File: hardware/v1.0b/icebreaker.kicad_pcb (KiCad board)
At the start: 4 copper layers, 73 x 37 mm, 128 parts, among them J1 Jumper, J10 Jumper, J11 Jumper, J12 Jumper, J13 Jumper, J14 Jumper, J15 Jumper, J16 Jumper, J17 Jumper, J18 Jumper, J19 Jumper, J2 Jumper, J20 Flash, J21 PMOD, J22 PMOD, J23 PMOD, J24 PMOD, J25 RGB Led, J26 5V AUX, J27 5V AUX, J28 CRESET, J3 Jumper, J4 Jumper, J5 Jumper, J6 Jumper, J7 Jumper, J8 Jumper, J9 Jumper, P1 pkl_USB_OTG, P2 UP, P3 UP, P4 UP, P5 UP, SW1 TACT, SW2 TACT, SW3 TACT, SW4 TACT, U1 93C46B-SOT-23-6, U2 3.3V, U3 1V2, U4 FT2232H, U5 W25Q, U6 ICE5LP4K-SG48, U7 12MHz

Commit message: Fixed pin header 3d models.
We had some of the models doubled up or not fully disabled. Now the TH
pin headers are all using KiCad V5 3d model locations and are all
disabled.

This fixes #23
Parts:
- removed the REF** at (42.2, 47.2)
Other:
- board text removed: "1Bitsquared"
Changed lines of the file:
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@@
-(kicad_pcb (version 20171130) (host pcbnew 5.0.0-fee4fd1~66~ubuntu18.04.1)
+(kicad_pcb (version 20171130) (host pcbnew 5.1.2-f72e74a~84~ubuntu18.04.1)
   (general
     (thickness 1.6)
-    (drawings 337)
+    (drawings 336)
     (tracks 1478)
     (zones 0)
-    (modules 128)
+    (modules 127)
     (nets 134)
   )
@@
     (zone_45_only yes)
     (trace_min 0.149)
-    (segment_width 0.2)
-    (edge_width 0.15)
     (via_size 0.5)
     (via_drill 0.3)
@@
     (uvia_min_size 0.2)
     (uvia_min_drill 0.1)
+    (edge_width 0.15)
+    (segment_width 0.2)
     (pcb_text_width 0.3)
     (pcb_text_size 1.5 1.5)
@@
     (pad_drill 0)
     (pad_to_mask_clearance 0.05)
+    (solder_mask_min_width 0.25)
     (aux_axis_origin 0 0)
     (grid_origin 55.1 47.5)
-    (visible_elements FFFFFF1F)
+    (visible_elements FFFFEF1F)
     (pcbplotparams
       (layerselection 0x010fc_ffffffff)
@@
       (rotate (xyz 0 0 0))
     )
+    (model ${KIPRJMOD}/../../lib/pkl/packages3d/pkl_buttons_switches.3dshapes/PTS810SJG250SMTRLFS.stp
+      (offset (xyz 0 0 1.5))
+      (scale (xyz 1 1 1))
+      (rotate (xyz -90 0 0))
+    )
   )
   (module pkl_buttons_switches:SW_SPST_3x4x2.5 (layer F.Cu)
@@
       (rotate (xyz 0 0 0))
     )
+    (model ${KIPRJMOD}/../../lib/pkl/packages3d/pkl_buttons_switches.3dshapes/PTS810SJG250SMTRLFS.stp
+      (offset (xyz 0 0 1.5))
+      (scale (xyz 1 1 1))
+      (rotate (xyz -90 0 0))
+    )
   )
   (module pkl_buttons_switches:SW_SPST_3x4x2.5 (layer F.Cu)
@@
       (rotate (xyz 0 0 0))
     )
+    (model ${KIPRJMOD}/../../lib/pkl/packages3d/pkl_buttons_switches.3dshapes/PTS810SJG250SMTRLFS.stp
+      (offset (xyz 0 0 1.5))
+      (scale (xyz 1 1 1))
+      (rotate (xyz -90 0 0))
+    )
   )
   (module pkl_buttons_switches:SW_SPST_3x4x2.5 (layer F.Cu)
@@
       (rotate (xyz 0 0 0))
     )
+    (model ${KIPRJMOD}/../../lib/pkl/packages3d/pkl_buttons_switches.3dshapes/PTS810SJG250SMTRLFS.stp
+      (offset (xyz 0 0 1.5))
+      (scale (xyz 1 1 1))
+      (rotate (xyz -90 0 0))
+    )
   )
   (module pkl_jumpers:J_NCNO_0903_30 (layer B.Cu)
@@
     (pad 7 thru_hole oval (at 0 15.24 90) (size 2.032 1.7272) (drill 1.016) (layers *.Cu *.Mask)
       (net 26 GND))
-    (model Pin_Headers.3dshapes/Pin_Header_Straight_1x07.wrl
-      (offset (xyz 0 -7.619999885559082 0))
+    (model ${KISYS3DMOD}/Connector_PinHeader_2.54mm.3dshapes/PinHeader_1x07_P2.54mm_Vertical.stepX
+      (at (xyz 0 0 0))
       (scale (xyz 1 1 1))
-      (rotate (xyz 0 0 90))
+      (rotate (xyz 0 0 0))
     )
   )
@@
     (pad 8 thru_hole oval (at 2.54 7.62 90) (size 1.7272 1.7272) (drill 1.016) (layers *.Cu *.Mask)
       (net 3 +3V3))
-    (model Pin_Headers.3dshapes/Pin_Header_Straight_2x04.wrl
-      (offset (xyz 1.269999980926514 -3.809999942779541 0))
+    (model ${KISYS3DMOD}/Connector_PinHeader_2.54mm.3dshapes/PinHeader_2x04_P2.54mm_Vertical.stepX
+      (at (xyz 0 0 0))
       (scale (xyz 1 1 1))
-      (rotate (xyz 0 0 90))
+      (rotate (xyz 0 0 0))
     )
   )
@@
     (pad 1 thru_hole rect (at 0 0 270) (size 1.7 1.7) (drill 1) (layers *.Cu *.Mask)
       (net 44 /iCE_CRESET))
-    (model ${KISYS3DMOD}/Connector_PinHeader_2.54mm.3dshapes/PinHeader_2x01_P2.54mm_VerticalX.wrl
+    (model ${KISYS3DMOD}/Connector_PinHeader_2.54mm.3dshapes/PinHeader_2x01_P2.54mm_Vertical.stepX
       (at (xyz 0 0 0))
       (scale (xyz 1 1 1))
@@
     (pad 2 thru_hole oval (at 2.54 0) (size 1.7272 1.7272) (drill 1.016) (layers *.Cu *.Mask)
       (net 26 GND))
-    (model Pin_Headers.3dshapes/Pin_Header_Straight_2x01.wrl
-      (offset (xyz 1.269999980926514 0 0))
+    (model ${KISYS3DMOD}/Connector_PinSocket_2.54mm.3dshapes/PinSocket_1x02_P2.54mm_Vertical.stepX
+      (at (xyz 0 0 0))
       (scale (xyz 1 1 1))
-      (rotate (xyz 0 0 90))
+      (rotate (xyz 0 0 -90))
     )
   )
@@
     (pad 2 thru_hole oval (at 2.54 0 90) (size 1.7272 1.7272) (drill 1.016) (layers *.Cu *.Mask)
       (net 26 GND))
-    (model Pin_Headers.3dshapes/Pin_Header_Straight_2x01.wrl
-      (offset (xyz 1.269999980926514 0 0))
+    (model ${KISYS3DMOD}/Connector_PinSocket_2.54mm.3dshapes/PinSocket_1x02_P2.54mm_Vertical.stepX
+      (at (xyz 0 0 0))
       (scale (xyz 1 1 1))
-      (rotate (xyz 0 0 90))
+      (rotate (xyz 0 0 -90))
     )
   )
@@
     (pad 7 thru_hole oval (at 2.54 12.7 180) (size 1.7272 1.7272) (drill 1.016) (layers *.Cu *.Mask)
       (net 107 /P2_7x))
-    (model Pin_Headers.3dshapes/Pin_Header_Straight_2x06.wrl
-      (offset (xyz 1.269999980926514 -6.349999904632568 0))
+    (model ${KISYS3DMOD}/Connector_PinHeader_2.54mm.3dshapes/PinHeader_2x06_P2.54mm_Horizontal.stepX
+      (at (xyz 0 0 0))
       (scale (xyz 1 1 1))
-      (rotate (xyz 0 0 90))
+      (rotate (xyz 0 0 0))
     )
   )
@@
     (pad 7 thru_hole oval (at 12.7 2.54 90) (size 1.7272 1.7272) (drill 1.016) (layers *.Cu *.Mask)
       (net 107 /P2_7x))
-    (model Socket_Strips.3dshapes/Socket_Strip_Straight_2x06.wrl
-      (offset (xyz 6.349999904632568 -1.269999980926514 0))
+    (model ${KISYS3DMOD}/Connector_PinSocket_2.54mm.3dshapes/PinSocket_2x06_P2.54mm_Horizontal.stepX
+      (at (xyz 0 0 0))
       (scale (xyz 1 1 1))
-      (rotate (xyz 0 0 180))
+      (rotate (xyz 0 0 -90))
     )
   )
@@
     (pad 6 thru_hole circle (at 0 0 180) (size 1.7272 1.7272) (drill 1.016) (layers *.Cu *.Mask)
       (net 3 +3V3))
-    (model dis${KISYS3DMOD}/Connector_PinSocket_2.54mm.3dshapes/PinSocket_2x06_P2.54mm_Horizontal.step
+    (model ${KISYS3DMOD}/Connector_PinSocket_2.54mm.3dshapes/PinSocket_2x06_P2.54mm_Horizontal.stepX
       (at (xyz 0 0 0))
       (scale (xyz 1 1 1))
@@
     (pad 7 thru_hole oval (at 12.7 2.54 180) (size 1.7272 1.7272) (drill 1.016) (layers *.Cu *.Mask)
       (net 93 /P1A7x))
-    (model dis${KISYS3DMOD}/Connector_PinSocket_2.54mm.3dshapes/PinSocket_2x06_P2.54mm_Horizontal.step
-      (offset (xyz 6.35 -1.27 0))
+    (model ${KISYS3DMOD}/Connector_PinSocket_2.54mm.3dshapes/PinSocket_2x06_P2.54mm_Horizontal.stepX
+      (at (xyz 0 0 0))
       (scale (xyz 1 1 1))
       (rotate (xyz 0 0 -90))
@@
       (net 6 /xFIFO_WKUP))
   )
-  (module pkl_logos:1b2_Logo_SilkS_5mm locked (layer B.Cu)
-    (at 42.2 47.2 180)
-    (fp_text reference REF** (at 0 -4 180) (layer B.Fab) hide
-      (effects (font (size 1 1) (thickness 0.15)) (justify mirror))
-    )
-    (fp_text value 1b2_Logo_SilkS_5mm (at 0 4 180) (layer B.Fab) hide
-      (effects (font (size 1 1) (thickness 0.15)) (justify mirror))
-    )
-    (fp_line (start -0.5 0.5) (end -0.5 2.5) (layer B.SilkS) (width 0.2))
-    (fp_line (start -0.5 2.5) (end -2.5 2.5) (layer B.SilkS) (width 0.2))
-    (fp_line (start -2.5 2.5) (end -2.5 0.5) (layer B.SilkS) (width 0.2))
-    (fp_line (start -2.5 0.5) (end -0.5 0.5) (layer B.SilkS) (width 0.2))
-    (fp_line (start -0.5 2.5) (end 0 2) (layer B.SilkS) (width 0.2))
-    (fp_line (start 0 2) (end 0 0) (layer B.SilkS) (width 0.2))
-    (fp_line (start 0 0) (end -0.5 0.5) (layer B.SilkS) (width 0.2))
-    (fp_line (start -2.5 0.5) (end -2 0) (layer B.SilkS) (width 0.2))
-    (fp_line (start -2 0) (end 0 0) (layer B.SilkS) (width 0.2))
-    (fp_line (start 2 2) (end 0.5 2) (layer B.SilkS) (width 0.2))
-    (fp_line (start 0.5 2) (end 0.5 -0.5) (layer B.SilkS) (width 0.2))
-    (fp_line (start 0.5 -0.5) (end -2 -0.5) (layer B.SilkS) (width 0.2))
-    (fp_line (start -2 -0.5) (end -2 -2) (layer B.SilkS) (width 0.2))
-    (fp_line (start -2 -2) (end 2 -2) (layer B.SilkS) (width 0.2))
-    (fp_line (start 2 -2) (end 2 2) (layer B.SilkS) (width 0.2))
-    (fp_line (start 2 2) (end 2.5 1.5) (layer B.SilkS) (width 0.2))
-    (fp_line (start 2.5 1.5) (end 2.5 -2.5) (layer B.SilkS) (width 0.2))
-    (fp_line (start 2.5 -2.5) (end 2 -2) (layer B.SilkS) (width 0.2))
-    (fp_line (start -2 -2) (end -1.5 -2.5) (layer B.SilkS) (width 0.2))
-    (fp_line (start -1.5 -2.5) (end 2.5 -2.5) (layer B.SilkS) (width 0.2))
-  )
   (module pkl_dipol:R_Array_Convex_4x0402 (layer F.Cu)
     (at 57.105546 43.866206 135)
@@
   (module pkl_connectors:Connector_USB_Micro_B_SMD locked (layer F.Cu)
     (at 31.5 47.5 180)
+    (attr smd)
     (fp_text reference P1 (at 4 0 270) (layer F.Fab)
       (effects (font (size 1 1) (thickness 0.15)))
@@
     (effects (font (size 0.75 0.75) (thickness 0.1875)))
   )
-  (gr_text 1Bitsquared (at 42.1 51) (layer B.SilkS)
-    (effects (font (size 1 1) (thickness 0.25)) (justify mirror))
-  )
   (gr_text CDONE (at 56.7 56.7) (layer F.SilkS)

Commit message: Added more legend silkscreen to ears.
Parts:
- added REF**: 1b2_Logo_SilkS_5mm, pkl_logos:1b2_Logo_SilkS_5mm, B.Cu at (42.2, 47.2)
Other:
- board text added: "1Bitsquared"
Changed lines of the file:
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@@
   (general
     (thickness 1.6)
-    (drawings 336)
+    (drawings 337)
     (tracks 1478)
     (zones 0)
-    (modules 127)
+    (modules 128)
     (nets 134)
   )
@@
     (add_net "Net-(U7-Pad2)")
   )
+  (module pkl_logos:1b2_Logo_SilkS_5mm locked (layer B.Cu)
+    (at 42.2 47.2 180)
+    (fp_text reference REF** (at 0 -4 180) (layer B.Fab) hide
+      (effects (font (size 1 1) (thickness 0.15)) (justify mirror))
+    )
+    (fp_text value 1b2_Logo_SilkS_5mm (at 0 4 180) (layer B.Fab) hide
+      (effects (font (size 1 1) (thickness 0.15)) (justify mirror))
+    )
+    (fp_line (start -0.5 0.5) (end -0.5 2.5) (layer B.SilkS) (width 0.2))
+    (fp_line (start -0.5 2.5) (end -2.5 2.5) (layer B.SilkS) (width 0.2))
+    (fp_line (start -2.5 2.5) (end -2.5 0.5) (layer B.SilkS) (width 0.2))
+    (fp_line (start -2.5 0.5) (end -0.5 0.5) (layer B.SilkS) (width 0.2))
+    (fp_line (start -0.5 2.5) (end 0 2) (layer B.SilkS) (width 0.2))
+    (fp_line (start 0 2) (end 0 0) (layer B.SilkS) (width 0.2))
+    (fp_line (start 0 0) (end -0.5 0.5) (layer B.SilkS) (width 0.2))
+    (fp_line (start -2.5 0.5) (end -2 0) (layer B.SilkS) (width 0.2))
+    (fp_line (start -2 0) (end 0 0) (layer B.SilkS) (width 0.2))
+    (fp_line (start 2 2) (end 0.5 2) (layer B.SilkS) (width 0.2))
+    (fp_line (start 0.5 2) (end 0.5 -0.5) (layer B.SilkS) (width 0.2))
+    (fp_line (start 0.5 -0.5) (end -2 -0.5) (layer B.SilkS) (width 0.2))
+    (fp_line (start -2 -0.5) (end -2 -2) (layer B.SilkS) (width 0.2))
+    (fp_line (start -2 -2) (end 2 -2) (layer B.SilkS) (width 0.2))
+    (fp_line (start 2 -2) (end 2 2) (layer B.SilkS) (width 0.2))
+    (fp_line (start 2 2) (end 2.5 1.5) (layer B.SilkS) (width 0.2))
+    (fp_line (start 2.5 1.5) (end 2.5 -2.5) (layer B.SilkS) (width 0.2))
+    (fp_line (start 2.5 -2.5) (end 2 -2) (layer B.SilkS) (width 0.2))
+    (fp_line (start -2 -2) (end -1.5 -2.5) (layer B.SilkS) (width 0.2))
+    (fp_line (start -1.5 -2.5) (end 2.5 -2.5) (layer B.SilkS) (width 0.2))
+  )
   (module pkl_buttons_switches:SW_SPST_3x4x2.5 (layer F.Cu)
     (at 99.4 40.7)
@@
     )
   )
+  (gr_text 1Bitsquared (at 42.1 51) (layer B.SilkS)
+    (effects (font (size 1 1) (thickness 0.25)) (justify mirror))
+  )
   (gr_text 1V8 (at 55.5 47 315) (layer B.SilkS)

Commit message: Replaced/added the null logo to the boards.
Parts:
- REF**: value 1b2_Logo_SilkS_5mm -> null_Logo_SilkS_5mm; footprint pkl_logos:1b2_Logo_SilkS_5mm -> pkl_logos:null_Logo_SilkS_5mm
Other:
- board text added: "NULL"
- board text removed: "1Bitsquared"
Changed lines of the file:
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@@
-(kicad_pcb (version 20171130) (host pcbnew 5.1.2-f72e74a~84~ubuntu18.04.1)
+(kicad_pcb (version 20171130) (host pcbnew 5.1.5-52549c5~86~ubuntu19.10.1)
   (general
     (thickness 1.6)
@@
     (add_net "Net-(U7-Pad2)")
   )
-  (module pkl_logos:1b2_Logo_SilkS_5mm locked (layer B.Cu)
+  (module pkl_logos:null_Logo_SilkS_5mm locked (layer B.Cu)
     (at 42.2 47.2 180)
     (fp_text reference REF** (at 0 -4 180) (layer B.Fab) hide
       (effects (font (size 1 1) (thickness 0.15)) (justify mirror))
     )
-    (fp_text value 1b2_Logo_SilkS_5mm (at 0 4 180) (layer B.Fab) hide
+    (fp_text value null_Logo_SilkS_5mm (at 0 4 180) (layer B.Fab) hide
       (effects (font (size 1 1) (thickness 0.15)) (justify mirror))
     )
-    (fp_line (start -0.5 0.5) (end -0.5 2.5) (layer B.SilkS) (width 0.2))
-    (fp_line (start -0.5 2.5) (end -2.5 2.5) (layer B.SilkS) (width 0.2))
-    (fp_line (start -2.5 2.5) (end -2.5 0.5) (layer B.SilkS) (width 0.2))
-    (fp_line (start -2.5 0.5) (end -0.5 0.5) (layer B.SilkS) (width 0.2))
-    (fp_line (start -0.5 2.5) (end 0 2) (layer B.SilkS) (width 0.2))
-    (fp_line (start 0 2) (end 0 0) (layer B.SilkS) (width 0.2))
-    (fp_line (start 0 0) (end -0.5 0.5) (layer B.SilkS) (width 0.2))
-    (fp_line (start -2.5 0.5) (end -2 0) (layer B.SilkS) (width 0.2))
-    (fp_line (start -2 0) (end 0 0) (layer B.SilkS) (width 0.2))
-    (fp_line (start 2 2) (end 0.5 2) (layer B.SilkS) (width 0.2))
-    (fp_line (start 0.5 2) (end 0.5 -0.5) (layer B.SilkS) (width 0.2))
-    (fp_line (start 0.5 -0.5) (end -2 -0.5) (layer B.SilkS) (width 0.2))
-    (fp_line (start -2 -0.5) (end -2 -2) (layer B.SilkS) (width 0.2))
-    (fp_line (start -2 -2) (end 2 -2) (layer B.SilkS) (width 0.2))
-    (fp_line (start 2 -2) (end 2 2) (layer B.SilkS) (width 0.2))
-    (fp_line (start 2 2) (end 2.5 1.5) (layer B.SilkS) (width 0.2))
-    (fp_line (start 2.5 1.5) (end 2.5 -2.5) (layer B.SilkS) (width 0.2))
-    (fp_line (start 2.5 -2.5) (end 2 -2) (layer B.SilkS) (width 0.2))
-    (fp_line (start -2 -2) (end -1.5 -2.5) (layer B.SilkS) (width 0.2))
-    (fp_line (start -1.5 -2.5) (end 2.5 -2.5) (layer B.SilkS) (width 0.2))
+    (fp_arc (start -0.4 -0.2) (end -0.7 -0.2) (angle 180) (layer B.SilkS) (width 0.15))
+    (fp_line (start 1 -0.5) (end 1.5 -0.5) (layer B.SilkS) (width 0.15))
+    (fp_line (start 1 0.5) (end 1 -0.5) (layer B.SilkS) (width 0.15))
+    (fp_line (start 0.2 -0.5) (end 0.7 -0.5) (layer B.SilkS) (width 0.15))
+    (fp_line (start 0.2 0.5) (end 0.2 -0.5) (layer B.SilkS) (width 0.15))
+    (fp_line (start -0.1 0.5) (end -0.1 -0.2) (layer B.SilkS) (width 0.15))
+    (fp_line (start -0.7 0.5) (end -0.7 -0.2) (layer B.SilkS) (width 0.15))
+    (fp_line (start -1 -0.5) (end -1 0.5) (layer B.SilkS) (width 0.15))
+    (fp_line (start -1.5 0.5) (end -1 -0.5) (layer B.SilkS) (width 0.15))
+    (fp_line (start -1.5 -0.5) (end -1.5 0.5) (layer B.SilkS) (width 0.15))
+    (fp_line (start 2.5 2.5) (end -2.5 2.5) (layer B.SilkS) (width 0.2))
+    (fp_line (start -2.5 2.5) (end -2.5 -2.5) (layer B.SilkS) (width 0.2))
+    (fp_line (start 2.5 2.5) (end 2.5 -2.5) (layer B.SilkS) (width 0.2))
+    (fp_line (start -2.5 -2.5) (end 2.5 -2.5) (layer B.SilkS) (width 0.2))
   )
   (module pkl_buttons_switches:SW_SPST_3x4x2.5 (layer F.Cu)
@@
     )
   )
-  (gr_text 1Bitsquared (at 42.1 51) (layer B.SilkS)
+  (gr_text NULL (at 42.1 51) (layer B.SilkS)
     (effects (font (size 1 1) (thickness 0.25)) (justify mirror))
   )

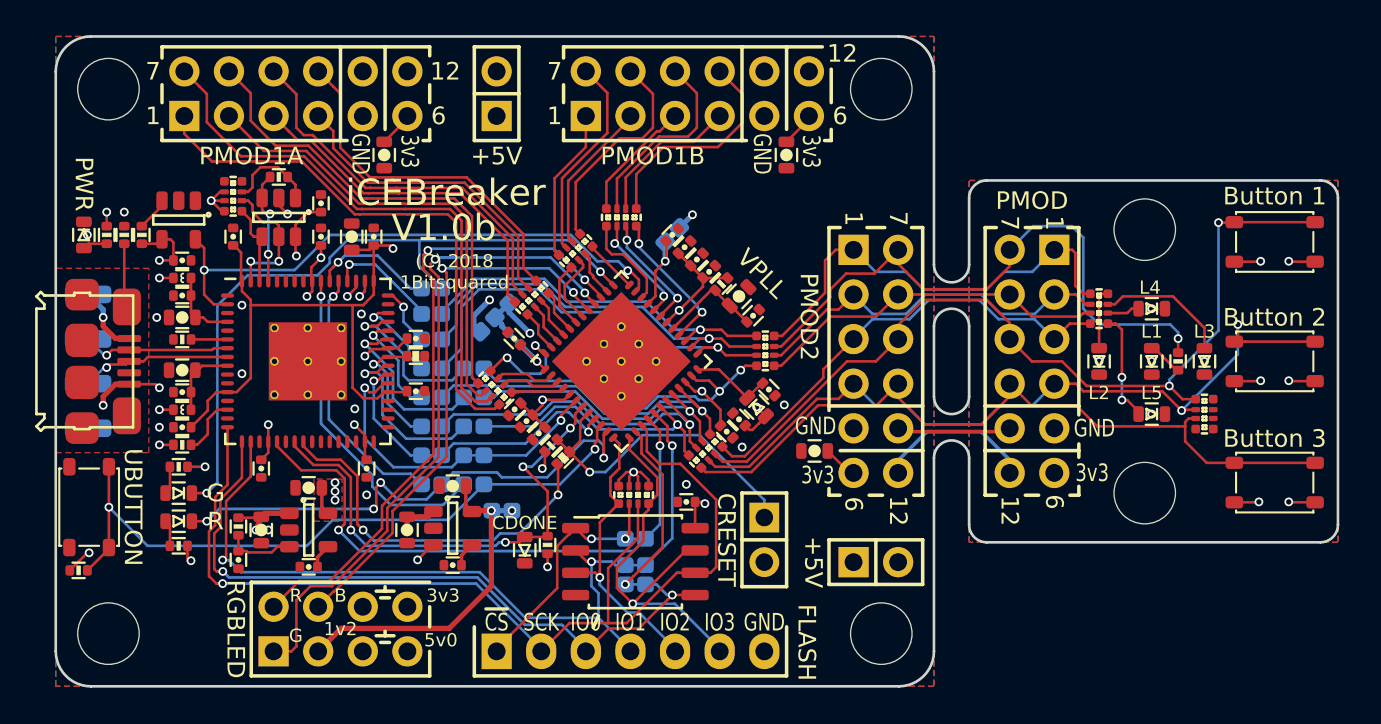
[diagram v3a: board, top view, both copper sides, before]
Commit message: Updated all design files to KiCad V8.0.6.
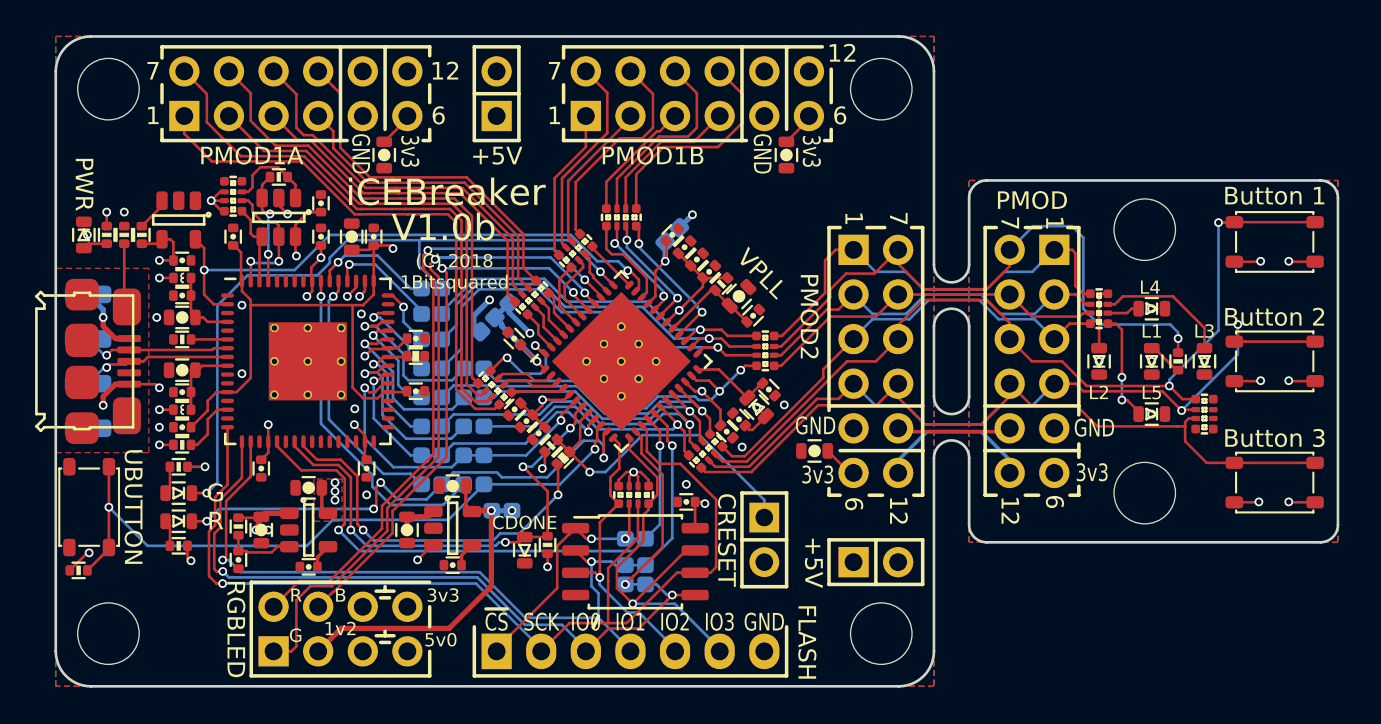
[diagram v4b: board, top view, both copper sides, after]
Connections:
- net /FLASH_~HLD~|~RST~|IO3 renamed /FLASH_~{HLD}|~{RST}|IO3
- net /FLASH_~WP~|IO2 renamed /FLASH_~{WP}|IO2
- net /xFIFO_~RD renamed /xFIFO_~{RD}
- net /xFIFO_~RXF renamed /xFIFO_~{RXF}
- net /xFIFO_~TXE renamed /xFIFO_~{TXE}
- net /xFIFO_~WR renamed /xFIFO_~{WR}
- net /~BUTTON renamed /~{BUTTON}
- net /~LEDG renamed /~{LEDG}
- net /~LEDR renamed /~{LEDR}
- net /~LED_BLU renamed /~{LED_BLU}
- net /~LED_GRN renamed /~{LED_GRN}
- net /~LED_RED renamed /~{LED_RED}
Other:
- net class Default removed
- board text added: "~{CS}"
- board text removed: "~CS"
